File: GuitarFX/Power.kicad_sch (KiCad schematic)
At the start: 8 parts, among them J1 Jack-DC, U3 NCP718xSN500, U4 NCP1117-3.3_SOT223

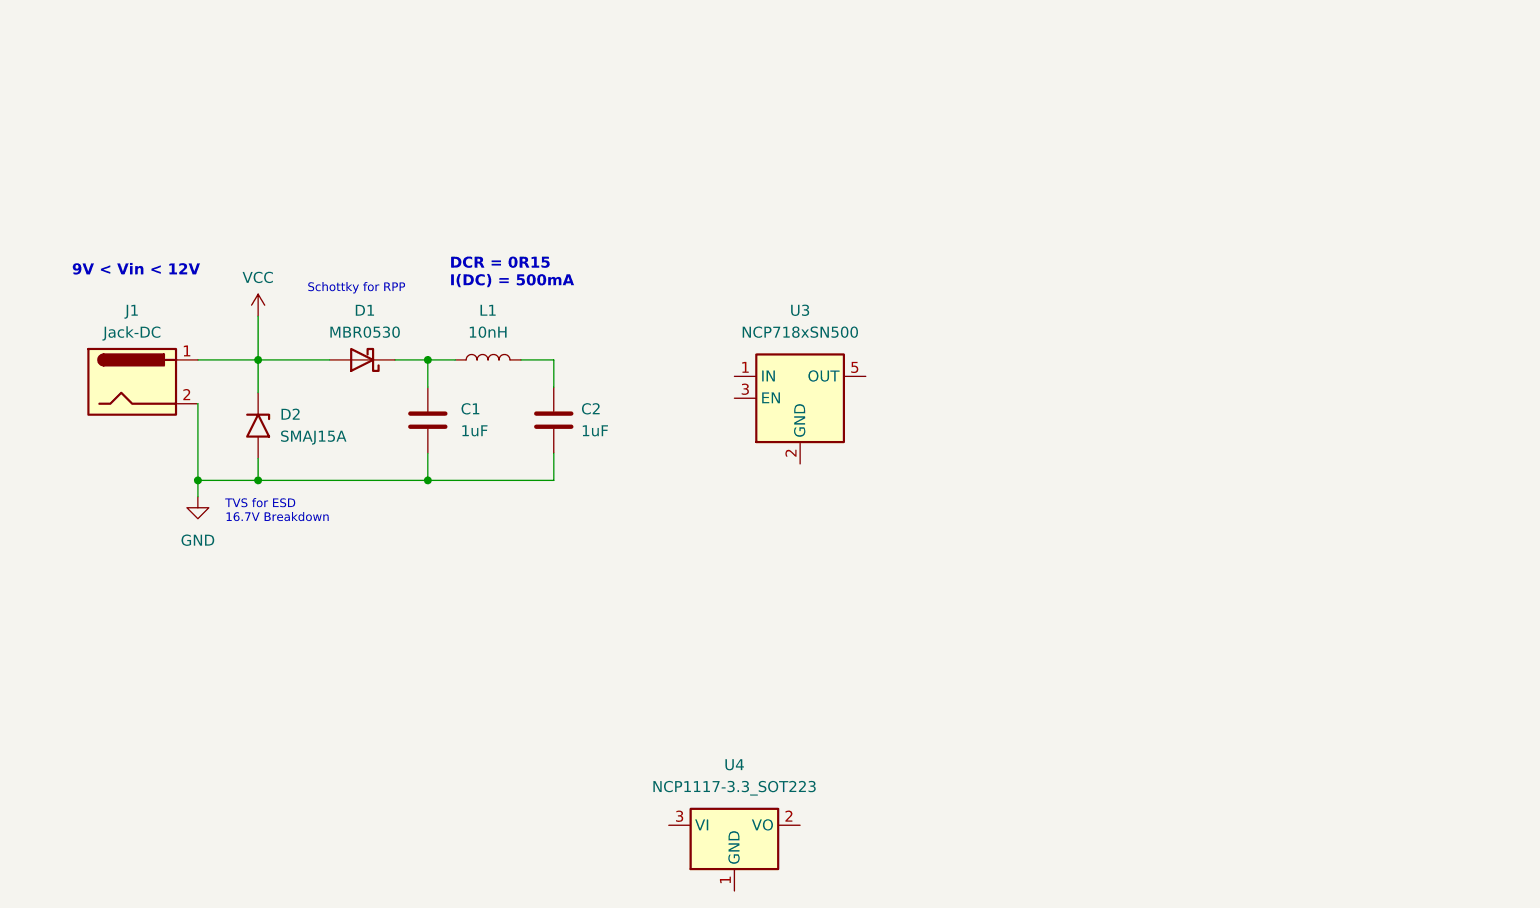
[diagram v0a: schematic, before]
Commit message: Finished power schematic
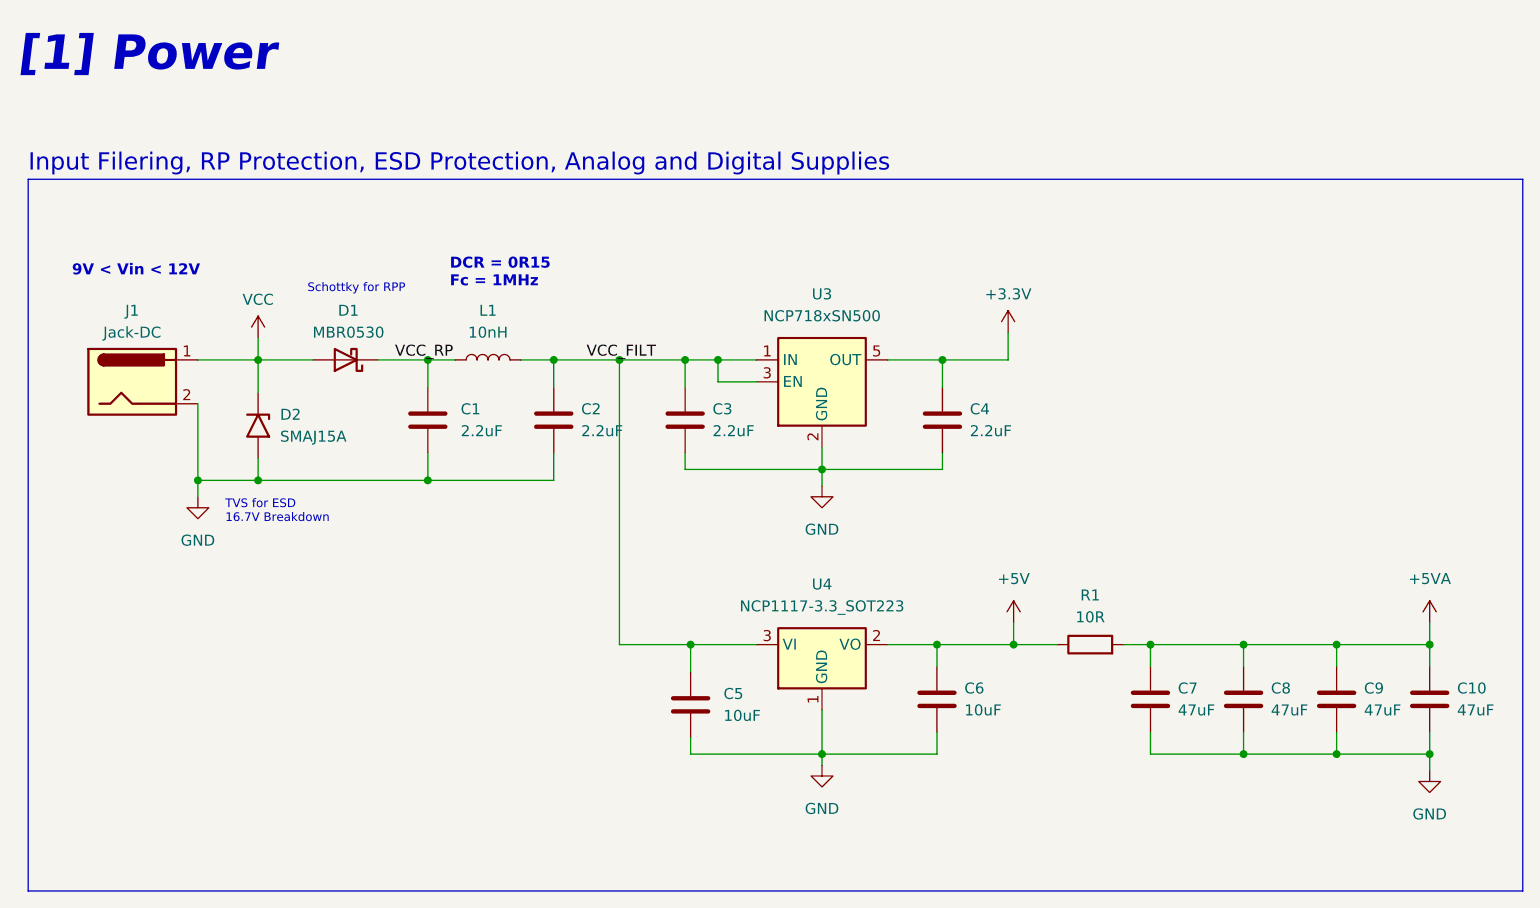
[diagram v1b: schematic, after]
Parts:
- added C10, C7, C8, C9: 47uF, symbol Device:C
- added C3, C4: 2.2uF, symbol Device:C
- added C5, C6: 10uF, symbol Device:C
- added R1: 10R, symbol Device:R
- C1, C2: value 1uF -> 2.2uF
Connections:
- net GND: now also U3.2 (GND), U4.1 (GND), C10.2, C3.2, C4.2, C5.2, C6.2, C7.2, C8.2, C9.2
- net +5V: now reaches U4.2 (VO)
- net +5V: now also C6.1, R1.1
- net VCC_FILT: now reaches U4.3 (VI)
- net VCC_FILT: now also C2.1, L1.2, U3.1 (IN), U3.3 (EN), C3.1, C5.1
- net VCC_RP: now reaches C1.1, D1.1 (K), L1.1
- net +3.3V: now reaches U3.5 (OUT)
- net +3.3V: now also C4.1
- new net +5VA: C10.1, C7.1, C8.1, C9.1, R1.2
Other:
- note added: "DCR = 0R15 Fc = 1MHz"
- note added: "Input Filering, RP Protection, ESD Protection, Analog and Digital Supplies"
- note added: "[1] Power"
- note removed: "DCR = 0R15 I(DC) = 500mA"
- moved on the sheet: D1, U3, U4

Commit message: Annotating schematic and fixing mistake
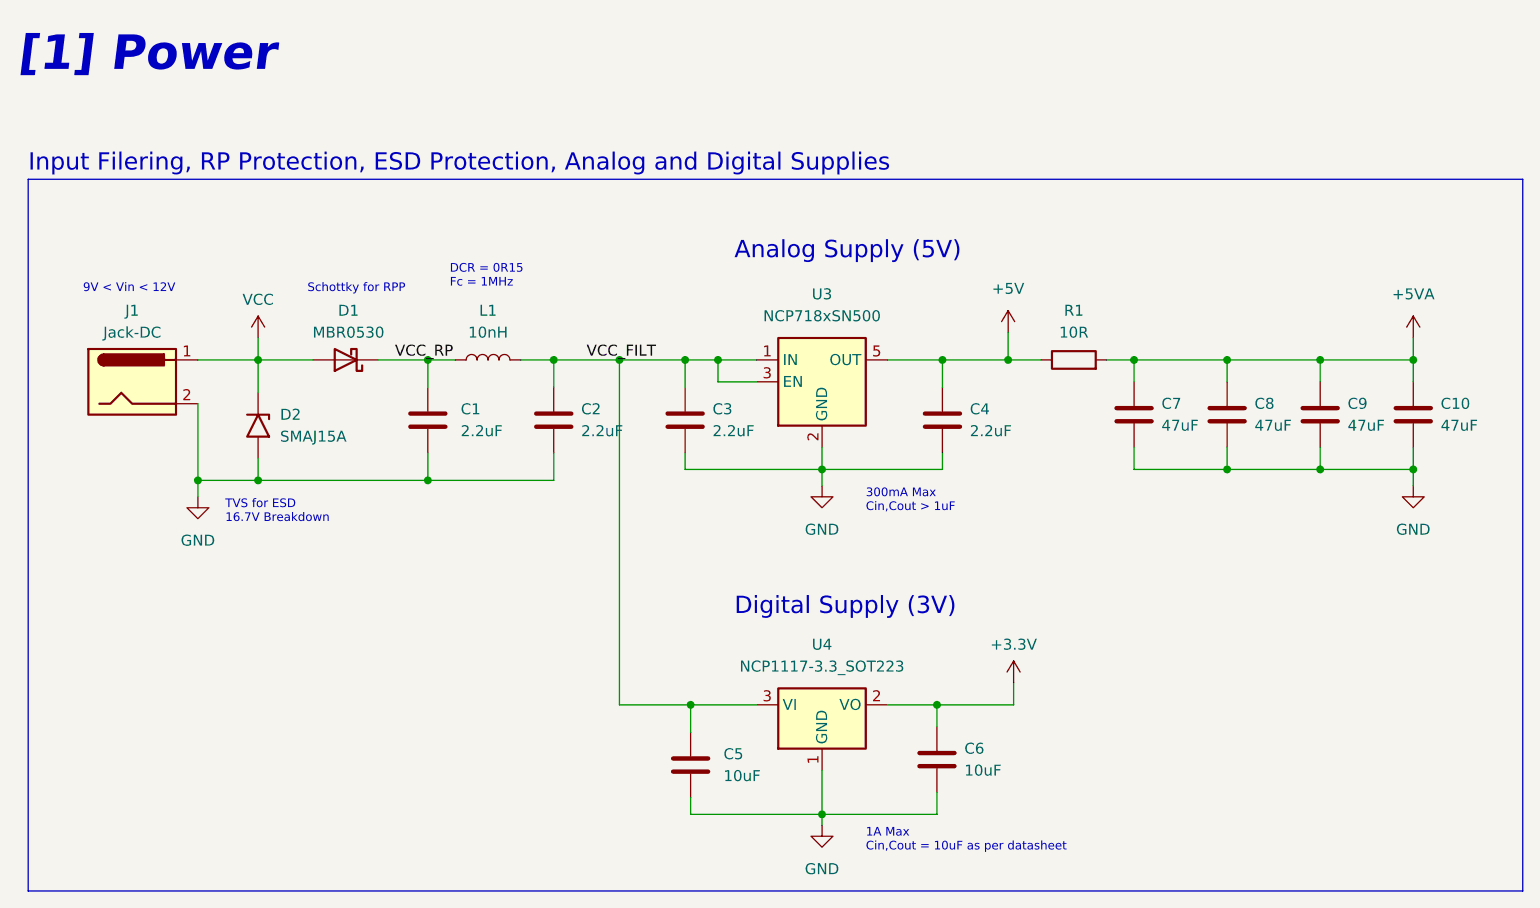
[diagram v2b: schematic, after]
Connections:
- net +3.3V: now also C6.1, U4.2 (VO); no longer C4.1, U3.5 (OUT)
- net +5V: now also C4.1, U3.5 (OUT); no longer C6.1, U4.2 (VO)
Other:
- note added: "1A Max Cin,Cout = 10uF as per datasheet"
- note added: "300mA Max Cin,Cout > 1uF"
- note added: "Analog Supply (5V)"
- note added: "Digital Supply (3V)"
- moved on the sheet: C5, C6, U4

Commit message: Added power led to power schematic
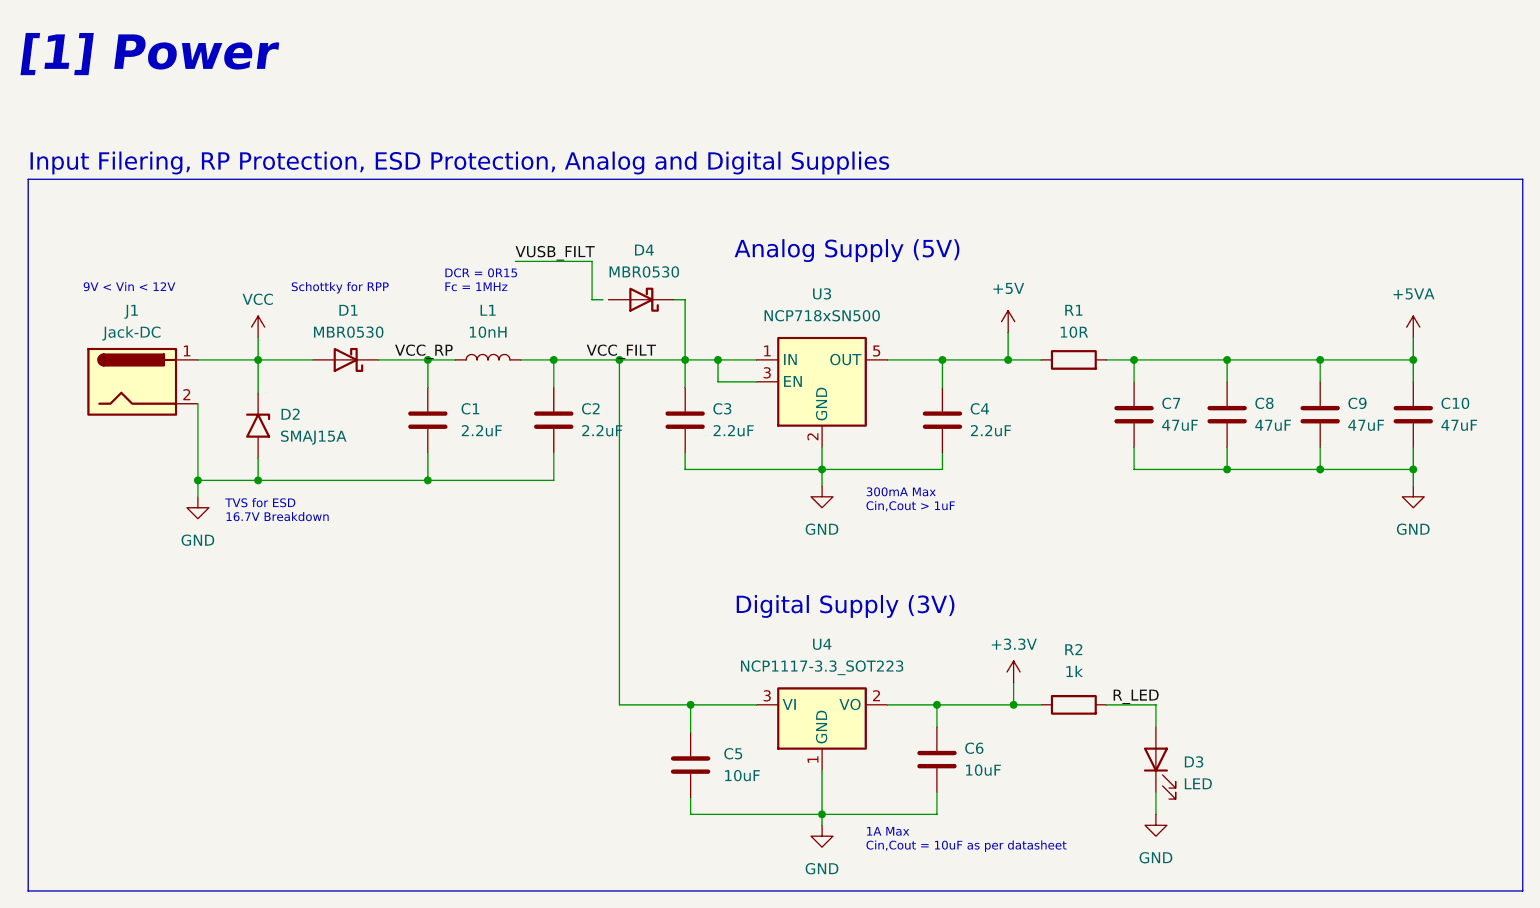
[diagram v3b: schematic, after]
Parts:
- added D3: LED, symbol Device:LED
- added D4: MBR0530, Diode_SMD:D_SOD-123, symbol Diode:MBR0530
- added R2: 1k, symbol Device:R
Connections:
- net +3.3V: now also R2.1
- net GND: now also D3.1 (K)
- net VCC_FILT: now also D4.1 (K)
- new net R_LED: D3.2 (A), R2.2
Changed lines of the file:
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@@
   (junction (at 117.475 62.865) (diameter 0) (color 0 0 0 0)
   )
+  (junction (at 155.575 102.87) (diameter 0) (color 0 0 0 0)
+  )
   (junction (at 87.63 76.835) (diameter 0) (color 0 0 0 0)
   )
@@
     (stroke (width 0) (type default))
   )
+  (wire (pts (xy 116.205 55.88) (xy 117.475 55.88))
+    (stroke (width 0) (type default))
+  )
   (wire (pts (xy 201.93 60.325) (xy 201.93 62.865))
     (stroke (width 0) (type default))
@@
     (stroke (width 0) (type default))
   )
+  (wire (pts (xy 117.475 55.88) (xy 117.475 62.865))
+    (stroke (width 0) (type default))
+  )
   (wire (pts (xy 117.475 62.865) (xy 117.475 66.04))
     (stroke (width 0) (type default))
@@
     (stroke (width 0) (type default))
   )
+  (wire (pts (xy 172.085 102.87) (xy 166.37 102.87))
+    (stroke (width 0) (type default))
+  )
   (wire (pts (xy 102.235 73.66) (xy 102.235 76.835))
     (stroke (width 0) (type default))
@@
     (stroke (width 0) (type default))
   )
+  (wire (pts (xy 172.085 113.03) (xy 172.085 115.57))
+    (stroke (width 0) (type default))
+  )
+  (wire (pts (xy 107.95 55.88) (xy 106.68 55.88))
+    (stroke (width 0) (type default))
+  )
   (wire (pts (xy 201.93 75.565) (xy 201.93 77.47))
     (stroke (width 0) (type default))
@@
     (stroke (width 0) (type default))
   )
+  (wire (pts (xy 155.575 102.87) (xy 158.75 102.87))
+    (stroke (width 0) (type default))
+  )
   (wire (pts (xy 67.945 62.865) (xy 67.945 60.325))
     (stroke (width 0) (type default))
   )
+  (wire (pts (xy 97.79 51.435) (xy 106.68 51.435))
+    (stroke (width 0) (type default))
+  )
   (wire (pts (xy 87.63 62.865) (xy 90.805 62.865))
     (stroke (width 0) (type default))
@@
     (stroke (width 0) (type default))
   )
+  (wire (pts (xy 106.68 55.88) (xy 106.68 51.435))
+    (stroke (width 0) (type default))
+  )
   (wire (pts (xy 166.37 62.865) (xy 169.545 62.865))
     (stroke (width 0) (type default))
@@
   )
   (wire (pts (xy 169.545 75.565) (xy 180.34 75.565))
+    (stroke (width 0) (type default))
+  )
+  (wire (pts (xy 172.085 105.41) (xy 172.085 102.87))
     (stroke (width 0) (type default))
   )
@@
     (effects (font (size 2 2)) (justify left bottom))
   )
-  (text "Schottky for RPP" (at 73.66 55.245 0)
+  (text "Schottky for RPP" (at 71.755 55.245 0)
     (effects (font (size 1 1)) (justify left bottom))
   )
@@
     (effects (font (size 1 1)) (justify left bottom))
   )
-  (text "DCR = 0R15\nFc = 1MHz" (at 90.17 54.61 0)
+  (text "DCR = 0R15\nFc = 1MHz" (at 89.535 55.245 0)
     (effects (font (size 1 1)) (justify left bottom))
   )
@@
     (effects (font (size 4 4) (thickness 2) bold italic) (justify left bottom))
   )
+  (label "R_LED" (at 167.005 102.87 0) (fields_autoplaced)
+    (effects (font (size 1.27 1.27)) (justify left bottom))
+  )
+  (label "VUSB_FILT" (at 97.79 51.435 0) (fields_autoplaced)
+    (effects (font (size 1.27 1.27)) (justify left bottom))
+  )
   (label "VCC_FILT" (at 106.045 62.865 0) (fields_autoplaced)
     (effects (font (size 1.27 1.27)) (justify left bottom))
@@
     (effects (font (size 1.27 1.27)) (justify left bottom))
   )
+  (symbol (lib_id "power:GND") (at 172.085 115.57 0) (unit 1)
+    (in_bom yes) (on_board yes) (dnp no) (fields_autoplaced)
+    (property "Reference" "#PWR09" (at 172.085 121.92 0)
+      (effects (font (size 1.27 1.27)) hide)
+    )
+    (property "Value" "GND" (at 172.085 120.65 0)
+      (effects (font (size 1.27 1.27)))
+    )
+    (property "Footprint" "" (at 172.085 115.57 0)
+      (effects (font (size 1.27 1.27)) hide)
+    )
+    (property "Datasheet" "" (at 172.085 115.57 0)
+      (effects (font (size 1.27 1.27)) hide)
+    )
+    (pin "1")
+    (instances
+      (project "GuitarFX"
+        (path "/4ab4bfc6-98ca-4cb1-8273-436b96035b51/171d6b95-1f9c-4c9d-954a-bc461d0cb77a"
+          (reference "#PWR09") (unit 1)
+        )
+      )
+    )
+  )
   (symbol (lib_id "Device:C") (at 169.545 69.215 0) (unit 1)
     (in_bom yes) (on_board yes) (dnp no) (fields_autoplaced)
@@
     )
   )
+  (symbol (lib_id "Diode:MBR0530") (at 112.395 55.88 180) (unit 1)
+    (in_bom yes) (on_board yes) (dnp no) (fields_autoplaced)
+    (property "Reference" "D4" (at 112.7125 50.165 0)
+      (effects (font (size 1.27 1.27)))
+    )
+    (property "Value" "MBR0530" (at 112.7125 52.705 0)
+      (effects (font (size 1.27 1.27)))
+    )
+    (property "Footprint" "Diode_SMD:D_SOD-123" (at 112.395 51.435 0)
+      (effects (font (size 1.27 1.27)) hide)
+    )
+    (property "Datasheet" "http://www.mccsemi.com/up_pdf/MBR0520~MBR0580(SOD123).pdf" (at 112.395 55.88 0)
+      (effects (font (size 1.27 1.27)) hide)
+    )
+    (pin "1")
+    (pin "2")
+    (instances
+      (project "GuitarFX"
+        (path "/4ab4bfc6-98ca-4cb1-8273-436b96035b51/171d6b95-1f9c-4c9d-954a-bc461d0cb77a"
+          (reference "D4") (unit 1)
+        )
+      )
+    )
+  )
   (symbol (lib_id "Device:C") (at 117.475 69.85 0) (unit 1)
     (in_bom yes) (on_board yes) (dnp no) (fields_autoplaced)
@@
         (path "/4ab4bfc6-98ca-4cb1-8273-436b96035b51/171d6b95-1f9c-4c9d-954a-bc461d0cb77a"
           (reference "C3") (unit 1)
+        )
+      )
+    )
+  )
+  (symbol (lib_id "Device:R") (at 162.56 102.87 90) (unit 1)
+    (in_bom yes) (on_board yes) (dnp no) (fields_autoplaced)
+    (property "Reference" "R2" (at 162.56 96.52 90)
+      (effects (font (size 1.27 1.27)))
+    )
+    (property "Value" "1k" (at 162.56 99.06 90)
+      (effects (font (size 1.27 1.27)))
+    )
+    (property "Footprint" "" (at 162.56 104.648 90)
+      (effects (font (size 1.27 1.27)) hide)
+    )
+    (property "Datasheet" "~" (at 162.56 102.87 0)
+      (effects (font (size 1.27 1.27)) hide)
+    )
+    (pin "1")
+    (pin "2")
+    (instances
+      (project "GuitarFX"
+        (path "/4ab4bfc6-98ca-4cb1-8273-436b96035b51/171d6b95-1f9c-4c9d-954a-bc461d0cb77a"
+          (reference "R2") (unit 1)
         )
       )
@@
         )
       )
+    )
+  )
+  (symbol (lib_id "Device:LED") (at 172.085 109.22 90) (unit 1)
+    (in_bom yes) (on_board yes) (dnp no) (fields_autoplaced)
+    (property "Reference" "D3" (at 175.26 109.5375 90)
+      (effects (font (size 1.27 1.27)) (justify right))
+    )
+    (property "Value" "LED" (at 175.26 112.0775 90)
+      (effects (font (size 1.27 1.27)) (justify right))
+    )
+    (property "Footprint" "" (at 172.085 109.22 0)
+      (effects (font (size 1.27 1.27)) hide)
+    )
+    (property "Datasheet" "~" (at 172.085 109.22 0)
+      (effects (font (size 1.27 1.27)) hide)
+    )
+    (pin "1")
+    (pin "2")
+    (instances
+      (project "GuitarFX"
+        (path "/4ab4bfc6-98ca-4cb1-8273-436b96035b51/171d6b95-1f9c-4c9d-954a-bc461d0cb77a"
+          (reference "D3") (unit 1)
+        )
+      )
